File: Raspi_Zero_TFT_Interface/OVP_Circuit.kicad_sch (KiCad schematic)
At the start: 0 parts

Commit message: First Pass Schematic Fixes for Power Management Board
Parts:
- added C11: 0.1u, Capacitor_SMD:C_0603_1608Metric_Pad1.08x0.95mm_HandSolder, symbol Device:C_Small
- added D6: NC, Diode_SMD:D_SOD-123, symbol Device:D_Zener
- added F1: 1.5 A Slow-Blow, Fuse:Fuse_0603_1608Metric, symbol Device:Fuse_Small
- added Q3: DMG3406L-7, Package_TO_SOT_SMD:SOT-23-3, symbol FrontEndPrototype_Rev1-rescue:DMG3406L
- added U8: TPS2400, Package_TO_SOT_SMD:SOT-23-5_HandSoldering, symbol FrontEndPrototype_Rev1-rescue:TPS2400
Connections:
- new net: Q3.1 (G), U8.4 (Gate)
- new net: F1.2, Q3.3 (D)
- new net GND: C11.2, D6.2 (A), U8.2 (GND)
- new net Vin: C11.1, D6.1 (K), F1.1, U8.5 (Vin)
- new net Vout: Q3.2 (S)
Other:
- note added: "30V Tolerant"
- note added: "Can possibly replace this circuit with a Transient Voltage Suppressor (TVS). This clamps voltage to safe level in case of transient spikes, but must rely on a fuse for prolonged surges."
- note added: "Components need to be at least 20V tolerant"
- note added: "NMOS Transistor Passes Input to Output with < 100 mOhm RdOn based on TPS2400 Gate Output"
- note added: "Zener Diode attenuates the voltage spike from an inductive power supply when load is disconnected. Most likely optional"

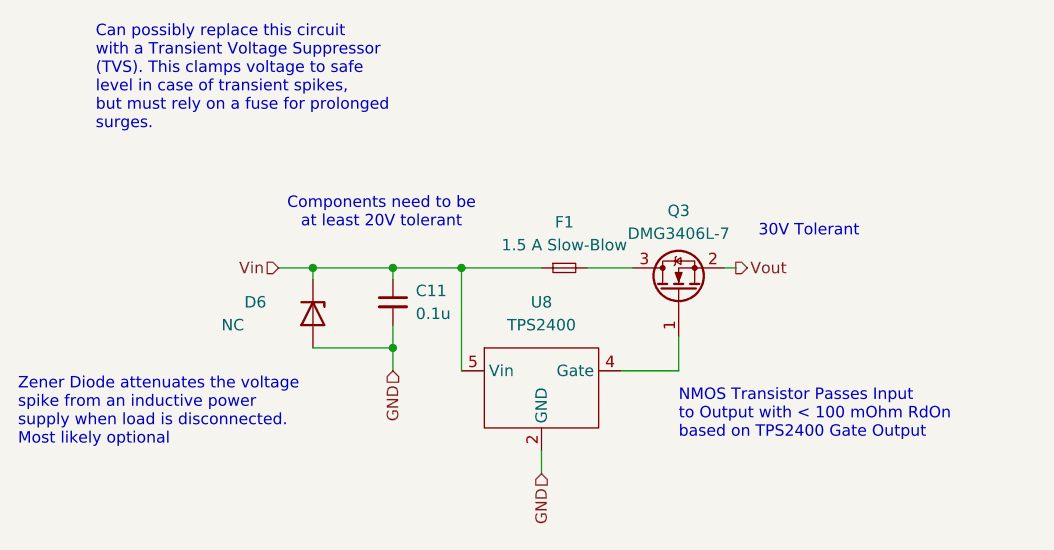
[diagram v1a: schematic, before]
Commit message: Finished Rasp Board PCB Routing
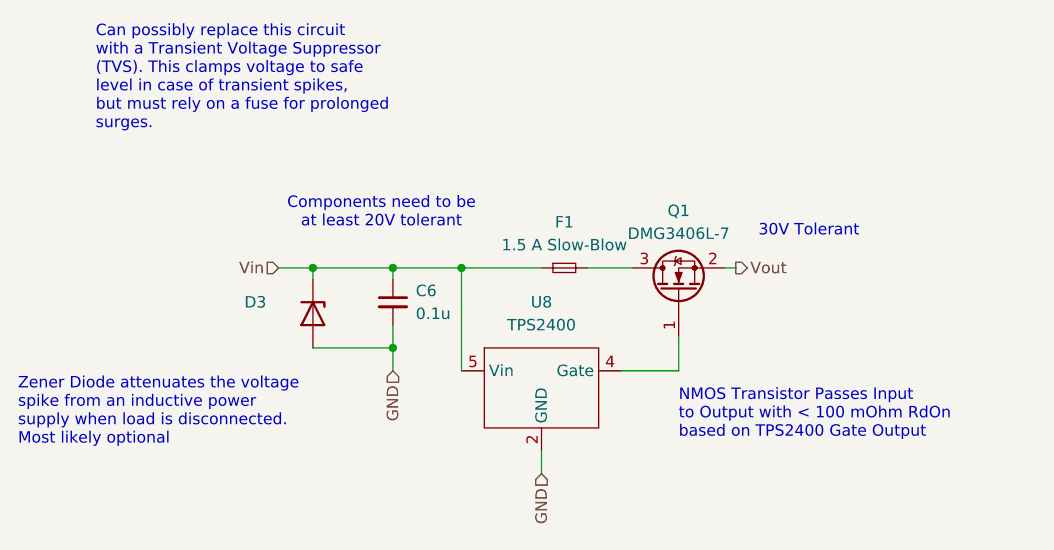
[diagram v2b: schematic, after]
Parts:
- renumbered C11 to C6, D6 to D3, Q3 to Q1
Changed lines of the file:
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@@
 		(dnp no)
 		(fields_autoplaced yes)
-		(property "Reference" "C11"
+		(property "Reference" "C6"
 			(at 71.12 53.3463 0)
 			(effects
@@
 		)
 		(pin "2"
+		)
+		(instances
+			(project "Raspi_Zero_TFT_Interface"
+				(path "/9fcf58ec-9ad6-40d8-a93b-d0fc15c15838/50d4a57d-354f-4afa-869e-4e71aa380902/3bad1f83-a2fe-4a97-b599-4c79fec87df7"
+					(reference "C6")
+					(unit 1)
+				)
+			)
 		)
 	)
@@
 		(on_board yes)
 		(dnp no)
-		(property "Reference" "D6"
+		(property "Reference" "D3"
 			(at 52.07 54.61 90)
 			(effects
@@
 				)
 				(justify left)
+				(hide yes)
 			)
 		)
@@
 		)
 		(pin "2"
+		)
+		(instances
+			(project "Raspi_Zero_TFT_Interface"
+				(path "/9fcf58ec-9ad6-40d8-a93b-d0fc15c15838/50d4a57d-354f-4afa-869e-4e71aa380902/3bad1f83-a2fe-4a97-b599-4c79fec87df7"
+					(reference "D3")
+					(unit 1)
+				)
+			)
 		)
 	)
@@
 		(dnp no)
 		(fields_autoplaced yes)
-		(property "Reference" "Q3"
+		(property "Reference" "Q1"
 			(at 100.33 44.45 90)
 			(effects
@@
 		(pin "3"
 		)
-	)
+		(instances
+			(project "Raspi_Zero_TFT_Interface"
+				(path "/9fcf58ec-9ad6-40d8-a93b-d0fc15c15838/50d4a57d-354f-4afa-869e-4e71aa380902/3bad1f83-a2fe-4a97-b599-4c79fec87df7"
+					(reference "Q1")
+					(unit 1)
+				)
+			)
+		)
+	)
